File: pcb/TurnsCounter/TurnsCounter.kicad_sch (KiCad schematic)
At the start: 39 parts, among them J1 Hall Sensors, U2 ATmega8A-A, U3 MAX7219, Y1 16MHz

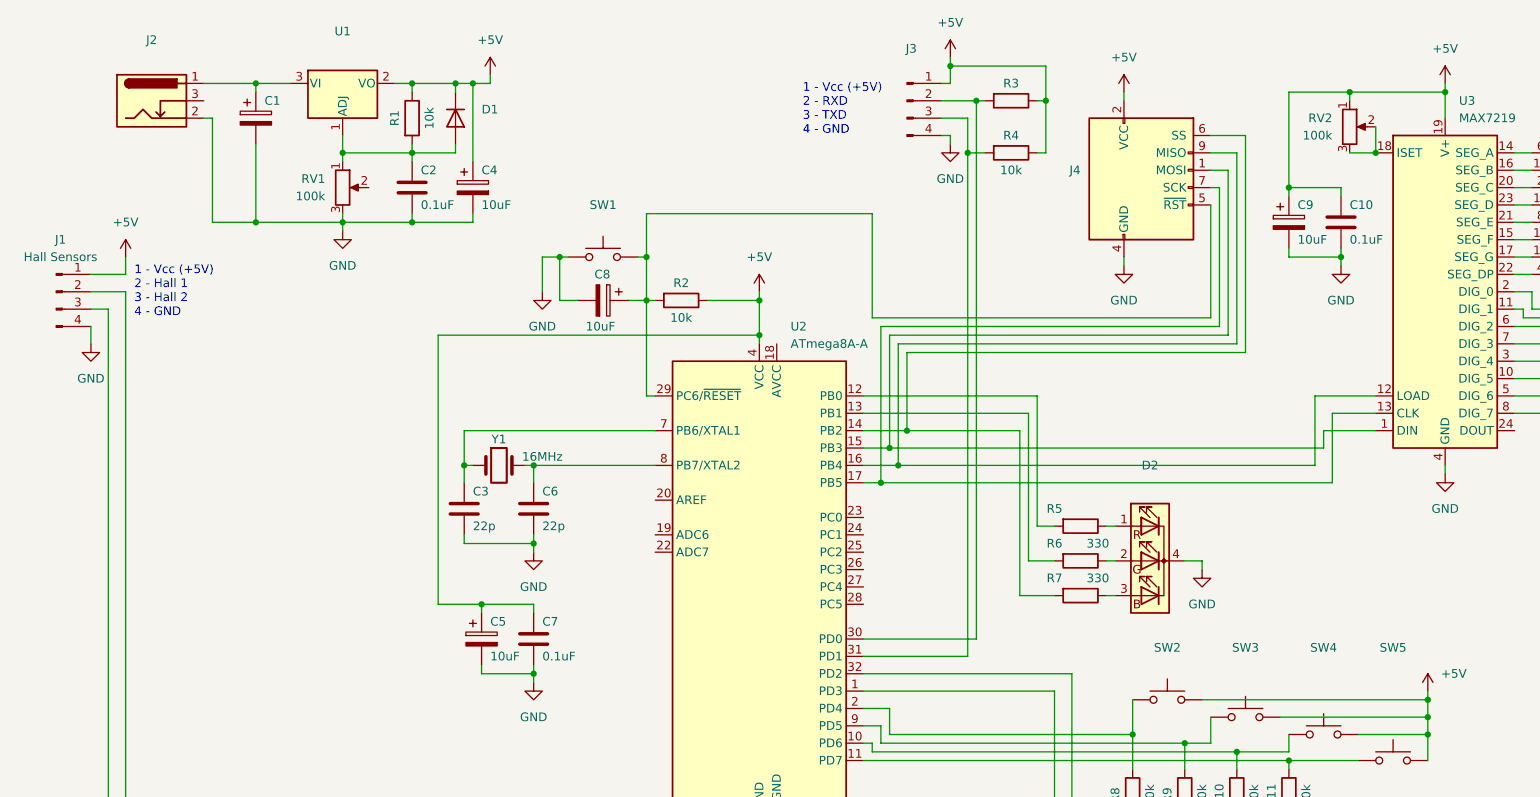
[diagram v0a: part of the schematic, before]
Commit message: pcb alpha, xtal deleted
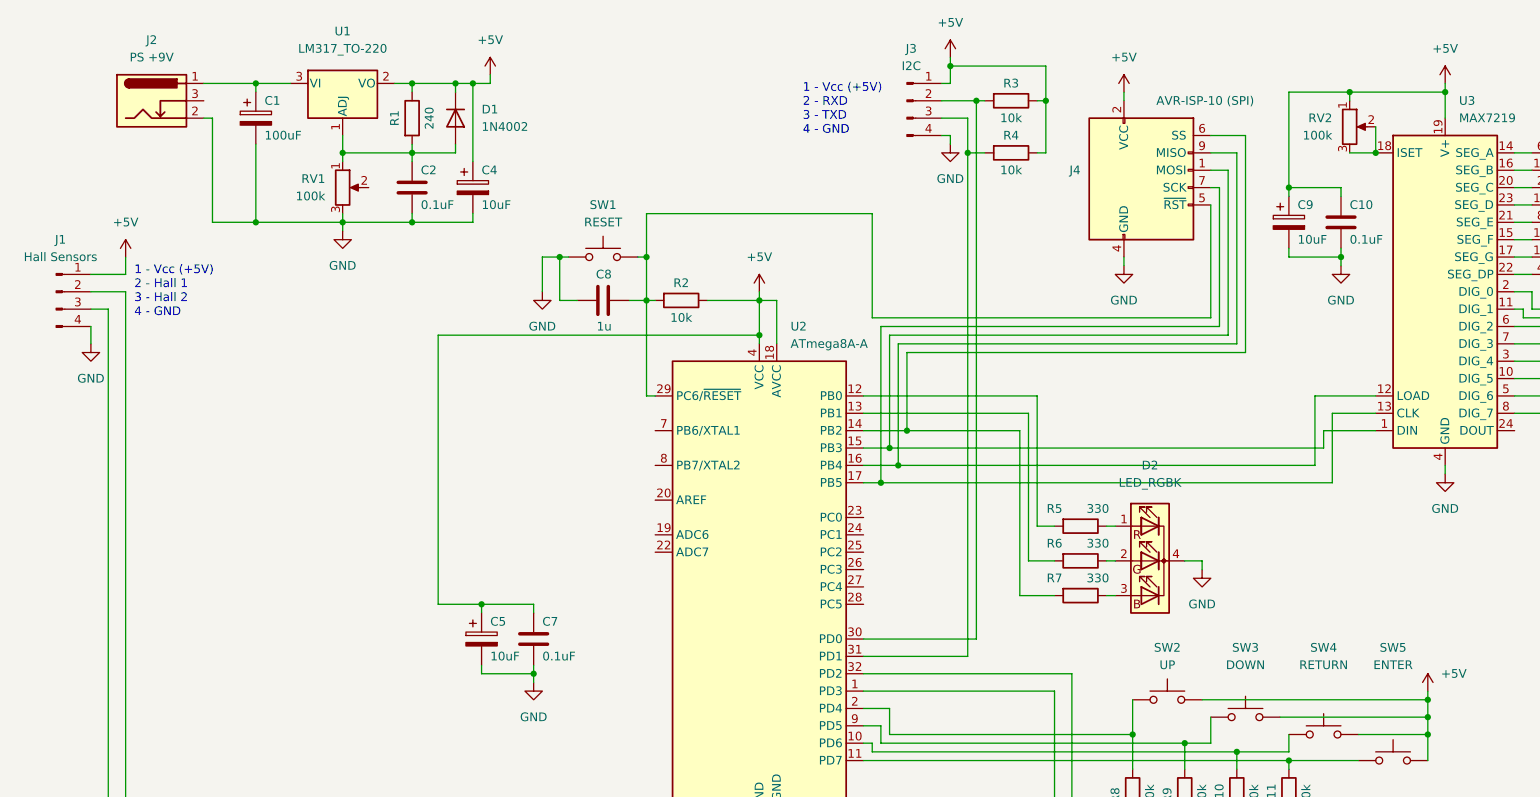
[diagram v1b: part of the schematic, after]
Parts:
- removed C3, C6: 22p, symbol Device:C
- removed C8: 10uF, symbol Device:C_Polarized
- removed Y1: 16MHz, symbol Device:Crystal
- added C8: 1u, Capacitor_SMD:C_0805_2012Metric_Pad1.18x1.45mm_HandSolder, symbol Device:C
- C1: value (none) -> 100uF; footprint (none) -> Capacitor_THT:CP_Radial_D5.0mm_P2.50mm
- C10, C2, C7: footprint (none) -> Capacitor_SMD:C_0805_2012Metric_Pad1.18x1.45mm_HandSolder
- C4, C5, C9: footprint (none) -> Capacitor_THT:CP_Radial_D5.0mm_P2.50mm
- D1: value (none) -> 1N4002; footprint (none) -> Diode_THT:D_DO-41_SOD81_P5.08mm_Vertical_KathodeUp
- D2: value (none) -> LED_RGBK; footprint (none) -> LED_THT:LED_D5.0mm-4_RGB_Staggered_Pins
- D3: footprint (none) -> Dawu_PCB_Library:ALS318A
- J1: footprint (none) -> Connector_PinHeader_2.54mm:PinHeader_1x04_P2.54mm_Vertical
- J2: value (none) -> PS +9V; footprint (none) -> Connector_BarrelJack:BarrelJack_Horizontal
- J3: value (none) -> I2C; footprint (none) -> Connector_PinHeader_2.54mm:PinHeader_1x04_P2.54mm_Vertical
- J4: value (none) -> AVR-ISP-10 (SPI); footprint (none) -> Connector_IDC:IDC-Header_2x05_P2.54mm_Vertical
- R1: value 10k -> 240; footprint (none) -> Resistor_SMD:R_0805_2012Metric_Pad1.20x1.40mm_HandSolder
- R10, R11, R2, R4, R6, R7, R8, R9: footprint (none) -> Resistor_SMD:R_0805_2012Metric_Pad1.20x1.40mm_HandSolder
- R3: value (none) -> 10k; footprint (none) -> Resistor_SMD:R_0805_2012Metric_Pad1.20x1.40mm_HandSolder
- R5: value (none) -> 330; footprint (none) -> Resistor_SMD:R_0805_2012Metric_Pad1.20x1.40mm_HandSolder
- RV1, RV2: footprint (none) -> Potentiometer_THT:Potentiometer_Bourns_3266W_Vertical
- SW1: value (none) -> RESET; footprint (none) -> Button_Switch_THT:SW_PUSH_6mm
- SW2: value (none) -> UP; footprint (none) -> Button_Switch_THT:SW_PUSH_6mm
- SW3: value (none) -> DOWN; footprint (none) -> Button_Switch_THT:SW_PUSH_6mm
- SW4: value (none) -> RETURN; footprint (none) -> Button_Switch_THT:SW_PUSH_6mm
- SW5: value (none) -> ENTER; footprint (none) -> Button_Switch_THT:SW_PUSH_6mm
- U1: value (none) -> LM317_TO-220; footprint (none) -> Package_TO_SOT_THT:TO-220-3_Vertical
- U3: footprint (none) -> Package_SO:SOIC-24W_7.5x15.4mm_P1.27mm
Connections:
- net +5V: now also U2.18 (AVCC)
- net GND: now also C8.1
- net at J4.5 (~{RST}), R2.2, SW1.2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: now also C8.2

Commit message: First PCB
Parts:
- removed C5: 10uF, Capacitor_THT:CP_Radial_D5.0mm_P2.50mm, symbol Device:C_Polarized
- added J10, J9: Conn_01x08_Male, Connector_PinSocket_2.54mm:PinSocket_1x08_P2.54mm_Vertical, symbol Connector:Conn_01x08_Male
- added J11: Conn_01x16_Male, Connector_PinSocket_2.54mm:PinSocket_1x16_P2.54mm_Vertical, symbol Connector:Conn_01x16_Male
- added J5: RGB Led, Connector_PinSocket_2.54mm:PinSocket_1x04_P2.54mm_Vertical, symbol Connector:Conn_01x04_Male
- added J6: RGB Led, Connector_PinSocket_2.54mm:PinSocket_1x04_P2.54mm_Vertical, symbol Connector:Conn_01x04_Female
- added J7: Conn_01x06_Male, Connector_PinSocket_2.54mm:PinSocket_1x06_P2.54mm_Vertical, symbol Connector:Conn_01x06_Male
- added J8: Keys, Connector_PinSocket_2.54mm:PinSocket_1x06_P2.54mm_Vertical, symbol Connector:Conn_01x06_Female
- SW3: value DOWN -> CENCEL
- SW4: value RETURN -> DOWN
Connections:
- net +5V: now also J7.1 (Pin_1); no longer SW2.2, SW3.2, SW4.2, SW5.2
- net GND: now also RV1.2, J5.4 (Pin_4), J7.6 (Pin_6); no longer D2.4 (K), R10.2, R11.2, R8.2, R9.2
- net at R8.1, SW2.1: now also J8.2 (Pin_2); no longer U2.2 (PD4)
- net at R11.1, SW5.1: now also J8.5 (Pin_5); no longer U2.11 (PD7)
- net at R9.1, SW3.1: now also J8.3 (Pin_3); no longer U2.9 (PD5)
- net at U2.12 (PB0): now also J5.1 (Pin_1); no longer R5.2
- net at R10.1, SW4.1: now also J8.4 (Pin_4); no longer U2.10 (PD6)
- net at J4.6 (SS), U2.14 (PB2): now also J5.3 (Pin_3); no longer R7.2
- net at U2.13 (PB1): now also J5.2 (Pin_2); no longer R6.2
- net at D3.10 (D): now also J11.9 (Pin_9); no longer U3.23 (SEG_D)
- net at U3.3 (DIG_4): now also J10.2 (Pin_2); no longer D3.11 (C6)
- net at D3.12 (G): now also J11.11 (Pin_11); no longer U3.17 (SEG_G)
- net at U3.10 (DIG_5): now also J10.7 (Pin_7); no longer D3.13 (C7)
- net at D3.14 (B): now also J11.13 (Pin_13); no longer U3.16 (SEG_B)
- net at U3.5 (DIG_6): now also J10.3 (Pin_3); no longer D3.15 (C8)
- net at D3.16 (F): now also J11.15 (Pin_15); no longer U3.15 (SEG_F)
- net at U3.8 (DIG_7): now also J10.6 (Pin_6); no longer D3.17 (C9)
- net at D3.2 (C): now also J11.1 (Pin_1); no longer U3.20 (SEG_C)
- net at U3.2 (DIG_0): now also J10.1 (Pin_1); no longer D3.3 (C2)
- net at D3.4 (H): now also J11.3 (Pin_3); no longer U3.22 (SEG_DP)
- net at U3.11 (DIG_1): now also J10.8 (Pin_8); no longer D3.5 (C3)
- net at D3.6 (A): now also J11.5 (Pin_5); no longer U3.14 (SEG_A)
- net at U3.6 (DIG_2): now also J10.4 (Pin_4); no longer D3.7 (C4)
- net at D3.8 (E): now also J11.7 (Pin_7); no longer U3.21 (SEG_E)
- net at U3.7 (DIG_3): now also J10.5 (Pin_5); no longer D3.9 (C5)
- new net: J8.1 (Pin_1), SW2.2, SW3.2, SW4.2, SW5.2
- new net: J8.6 (Pin_6), R10.2, R11.2, R8.2, R9.2
- new net: D2.4 (K), J6.4 (Pin_4)
- new net: J6.1 (Pin_1), R5.2
- new net: J6.2 (Pin_2), R6.2
- new net: J6.3 (Pin_3), R7.2
- new net: J7.2 (Pin_2), U2.2 (PD4)
- new net: J7.3 (Pin_3), U2.9 (PD5)
- new net: J7.4 (Pin_4), U2.10 (PD6)
- new net: J7.5 (Pin_5), U2.11 (PD7)
- new net: D3.11 (C6), J11.10 (Pin_10)
- new net: D3.13 (C7), J11.12 (Pin_12)
- new net: D3.15 (C8), J11.14 (Pin_14)
- new net: D3.17 (C9), J11.16 (Pin_16)
- new net: D3.3 (C2), J11.2 (Pin_2)
- new net: D3.5 (C3), J11.4 (Pin_4)
- new net: D3.7 (C4), J11.6 (Pin_6)
- new net: D3.9 (C5), J11.8 (Pin_8)
- new net: J9.1 (Pin_1), U3.14 (SEG_A)
- new net: J9.2 (Pin_2), U3.15 (SEG_F)
- new net: J9.3 (Pin_3), U3.16 (SEG_B)
- new net: J9.4 (Pin_4), U3.17 (SEG_G)
- new net: J9.5 (Pin_5), U3.20 (SEG_C)
- new net: J9.6 (Pin_6), U3.21 (SEG_E)
- new net: J9.7 (Pin_7), U3.22 (SEG_DP)
- new net: J9.8 (Pin_8), U3.23 (SEG_D)
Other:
- moved on the sheet: D2, D3, R10, R11, R5, R6, R7, R8, R9, SW2, SW3, SW4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

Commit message: pcb fin
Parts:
- SW1, SW2, SW3, SW4, SW5: footprint Button_Switch_THT:SW_PUSH_6mm -> Dawu_PCB_Library:SW_PUSH_6mm_2
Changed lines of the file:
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@@
     (property "Reference" "SW2" (id 0) (at 228.6 123.19 0))
     (property "Value" "UP" (id 1) (at 228.6 125.73 0))
-    (property "Footprint" "Button_Switch_THT:SW_PUSH_6mm" (id 2) (at 228.6 125.73 0)
+    (property "Footprint" "Dawu_PCB_Library:SW_PUSH_6mm_2" (id 2) (at 228.6 125.73 0)
       (effects (font (size 1.27 1.27)) hide)
     )
@@
     (property "Reference" "SW5" (id 0) (at 261.62 121.92 0))
     (property "Value" "ENTER" (id 1) (at 261.62 124.46 0))
-    (property "Footprint" "Button_Switch_THT:SW_PUSH_6mm" (id 2) (at 261.62 133.35 0)
+    (property "Footprint" "Dawu_PCB_Library:SW_PUSH_6mm_2" (id 2) (at 261.62 133.35 0)
       (effects (font (size 1.27 1.27)) hide)
     )
@@
     (property "Reference" "SW1" (id 0) (at 105.41 39.37 0))
     (property "Value" "RESET" (id 1) (at 105.41 41.91 0))
-    (property "Footprint" "Button_Switch_THT:SW_PUSH_6mm" (id 2) (at 105.41 41.91 0)
+    (property "Footprint" "Dawu_PCB_Library:SW_PUSH_6mm_2" (id 2) (at 105.41 41.91 0)
       (effects (font (size 1.27 1.27)) hide)
     )
@@
     (property "Reference" "SW4" (id 0) (at 251.46 123.19 0))
     (property "Value" "DOWN" (id 1) (at 251.46 125.73 0))
-    (property "Footprint" "Button_Switch_THT:SW_PUSH_6mm" (id 2) (at 251.46 130.81 0)
+    (property "Footprint" "Dawu_PCB_Library:SW_PUSH_6mm_2" (id 2) (at 251.46 130.81 0)
       (effects (font (size 1.27 1.27)) hide)
     )
@@
     (property "Reference" "SW3" (id 0) (at 240.03 123.19 0))
     (property "Value" "CENCEL" (id 1) (at 240.03 125.73 0))
-    (property "Footprint" "Button_Switch_THT:SW_PUSH_6mm" (id 2) (at 240.03 128.27 0)
+    (property "Footprint" "Dawu_PCB_Library:SW_PUSH_6mm_2" (id 2) (at 240.03 128.27 0)
       (effects (font (size 1.27 1.27)) hide)
     )
@@
     )
     (path "/23b2dc41-876d-4989-959c-9ac0f716ae8e"
-      (reference "SW1") (unit 1) (value "RESET") (footprint "Button_Switch_THT:SW_PUSH_6mm")
+      (reference "SW1") (unit 1) (value "RESET") (footprint "Dawu_PCB_Library:SW_PUSH_6mm_2")
     )
     (path "/15f658c0-5bdf-4e26-9161-da88936cf2de"
-      (reference "SW2") (unit 1) (value "UP") (footprint "Button_Switch_THT:SW_PUSH_6mm")
+      (reference "SW2") (unit 1) (value "UP") (footprint "Dawu_PCB_Library:SW_PUSH_6mm_2")
     )
     (path "/c17e3282-0c5b-4f7c-8012-1534b3848016"
-      (reference "SW3") (unit 1) (value "CENCEL") (footprint "Button_Switch_THT:SW_PUSH_6mm")
+      (reference "SW3") (unit 1) (value "CENCEL") (footprint "Dawu_PCB_Library:SW_PUSH_6mm_2")
     )
     (path "/a3014963-57ac-4f52-9d8a-e12715f885da"
-      (reference "SW4") (unit 1) (value "DOWN") (footprint "Button_Switch_THT:SW_PUSH_6mm")
+      (reference "SW4") (unit 1) (value "DOWN") (footprint "Dawu_PCB_Library:SW_PUSH_6mm_2")
     )
     (path "/1bc9f570-0523-4b44-a708-2a9ebac64f77"
-      (reference "SW5") (unit 1) (value "ENTER") (footprint "Button_Switch_THT:SW_PUSH_6mm")
+      (reference "SW5") (unit 1) (value "ENTER") (footprint "Dawu_PCB_Library:SW_PUSH_6mm_2")
     )
     (path "/17706b18-96a9-4d0e-9910-5d83d21cbb73"
